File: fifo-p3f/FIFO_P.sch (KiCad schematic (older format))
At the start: 101 parts, among them J1 Vin, J2 Jack-DC, J3 Screw_Terminal_01x08, J4 XWCLK, J5 XRCLK, J6 Conn_02x04_Odd_Even, J7 Start Trigger, J8 Vout, Q1 DMP3099L, SW1 Rotary_Encoder_61C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

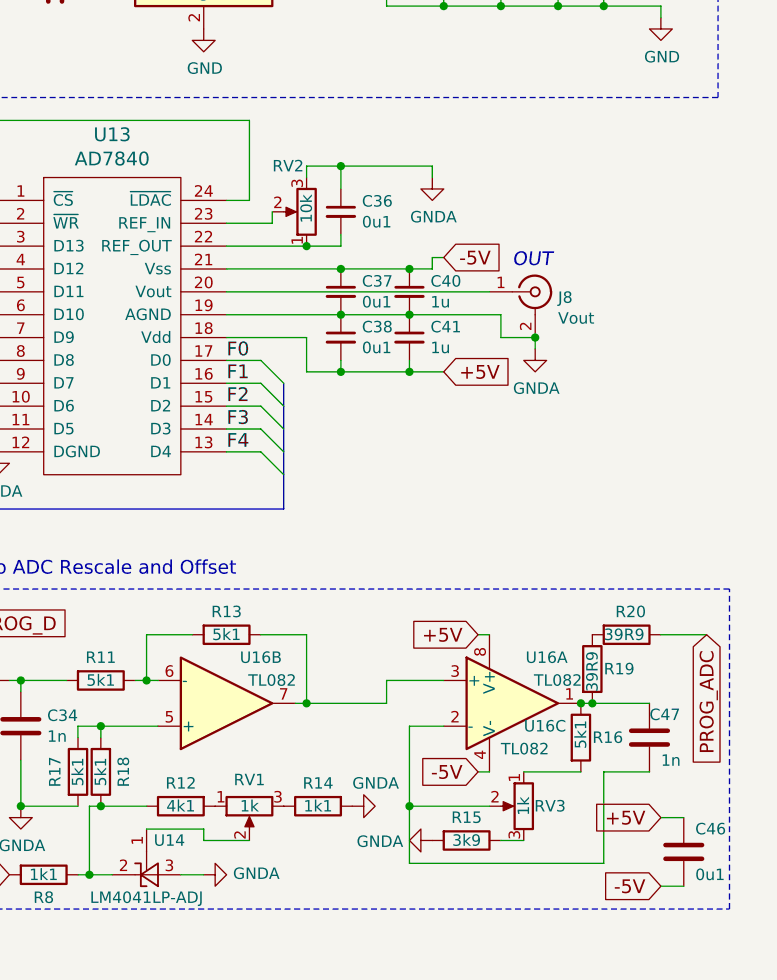
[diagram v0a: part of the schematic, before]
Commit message: Added assembly instructions, removed TeX logs, and reorganized docs
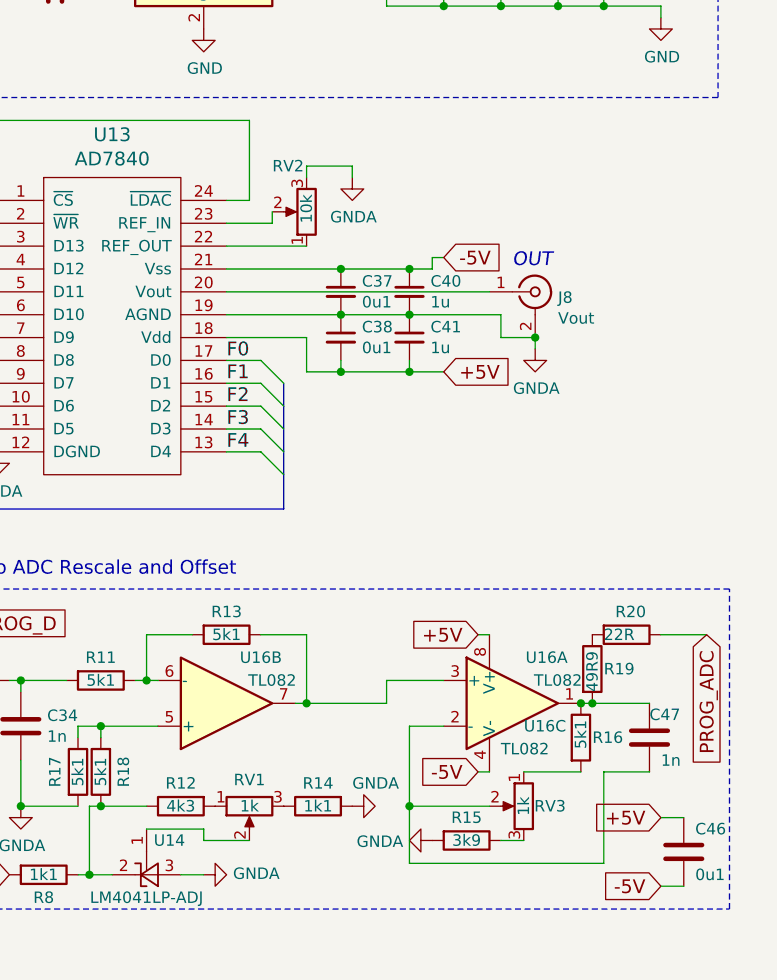
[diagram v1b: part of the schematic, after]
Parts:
- removed C36: 0u1, Capacitor_SMD:C_0805_2012Metric_Pad1.15x1.40mm_HandSolder, symbol Device:C_Small
- R12: value 4k1 -> 4k3
- R19: value 39R9 -> 49R9
- R20: value 39R9 -> 22R
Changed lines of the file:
@@
 Wire Wire Line
 	9200 4400 9550 4400
-$Comp
-L Device:C_Small C36
-U 1 1 5DB15B27
-P 9700 4250
-F 0 "C36" H 9792 4296 50  0000 L CNN
-F 1 "0u1" H 9792 4205 50  0000 L CNN
-F 2 "Capacitor_SMD:C_0805_2012Metric_Pad1.15x1.40mm_HandSolder" H 9700 4250 50  0001 C CNN
-F 3 "~" H 9700 4250 50  0001 C CNN
-	1    9700 4250
-	1    0    0    -1
-$EndComp
-Wire Wire Line
-	9550 4400 9700 4400
-Wire Wire Line
-	9700 4400 9700 4350
-Connection ~ 9550 4400
-Wire Wire Line
-	9700 4150 9700 4050
-Wire Wire Line
-	9700 4050 9550 4050
 Wire Wire Line
 	9550 4050 9550 4100
@@
 P 9000 6850
 F 0 "R12" V 8900 6850 50  0000 C CNN
-F 1 "4k1" V 9000 6850 50  0000 C CNN
+F 1 "4k3" V 9000 6850 50  0000 C CNN
 F 2 "Resistor_SMD:R_0805_2012Metric_Pad1.15x1.40mm_HandSolder" V 8930 6850 50  0001 C CNN
 F 3 "~" H 9000 6850 50  0001 C CNN
@@
 L power:GNDA #PWR054
 U 1 1 5E2B41BB
-P 10100 4100
-F 0 "#PWR054" H 10100 3850 50  0001 C CNN
-F 1 "GNDA" H 10105 3927 50  0000 C CNN
-F 2 "" H 10100 4100 50  0001 C CNN
-F 3 "" H 10100 4100 50  0001 C CNN
-	1    10100 4100
-	1    0    0    -1
-$EndComp
-Connection ~ 9700 4050
-Wire Wire Line
-	10100 4050 10100 4100
-Wire Wire Line
-	9700 4050 10100 4050
+P 9750 4100
+F 0 "#PWR054" H 9750 3850 50  0001 C CNN
+F 1 "GNDA" H 9755 3927 50  0000 C CNN
+F 2 "" H 9750 4100 50  0001 C CNN
+F 3 "" H 9750 4100 50  0001 C CNN
+	1    9750 4100
+	1    0    0    -1
+$EndComp
+Wire Wire Line
+	9750 4050 9750 4100
 Wire Bus Line
 	7950 5550 7750 5550
@@
 P 10800 6250
 F 0 "R19" H 10850 6250 50  0000 L CNN
-F 1 "39R9" V 10800 6150 50  0000 L CNN
+F 1 "49R9" V 10800 6150 50  0000 L CNN
 F 2 "Resistor_SMD:R_0805_2012Metric_Pad1.15x1.40mm_HandSolder" V 10730 6250 50  0001 C CNN
 F 3 "~" H 10800 6250 50  0001 C CNN
@@
 P 10950 6100
 F 0 "R20" V 10850 6050 50  0000 L CNN
-F 1 "39R9" V 10950 6000 50  0000 L CNN
+F 1 "22R" V 10950 6000 50  0000 L CNN
 F 2 "Resistor_SMD:R_0805_2012Metric_Pad1.15x1.40mm_HandSolder" V 10880 6100 50  0001 C CNN
 F 3 "~" H 10950 6100 50  0001 C CNN
@@
 Wire Wire Line
 	10300 6700 10350 6700
+Wire Wire Line
+	9550 4050 9750 4050
 Wire Bus Line
 	6650 6200 7550 6200
